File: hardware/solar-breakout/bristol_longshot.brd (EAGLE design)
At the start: 67 parts, among them U1 SPV1040, U2 SPV1040, U3 LT4054ES5-4.2, U4 TPS62243, U5 TPS62243, U6 TPS3808, U7 74LVC1G04GW

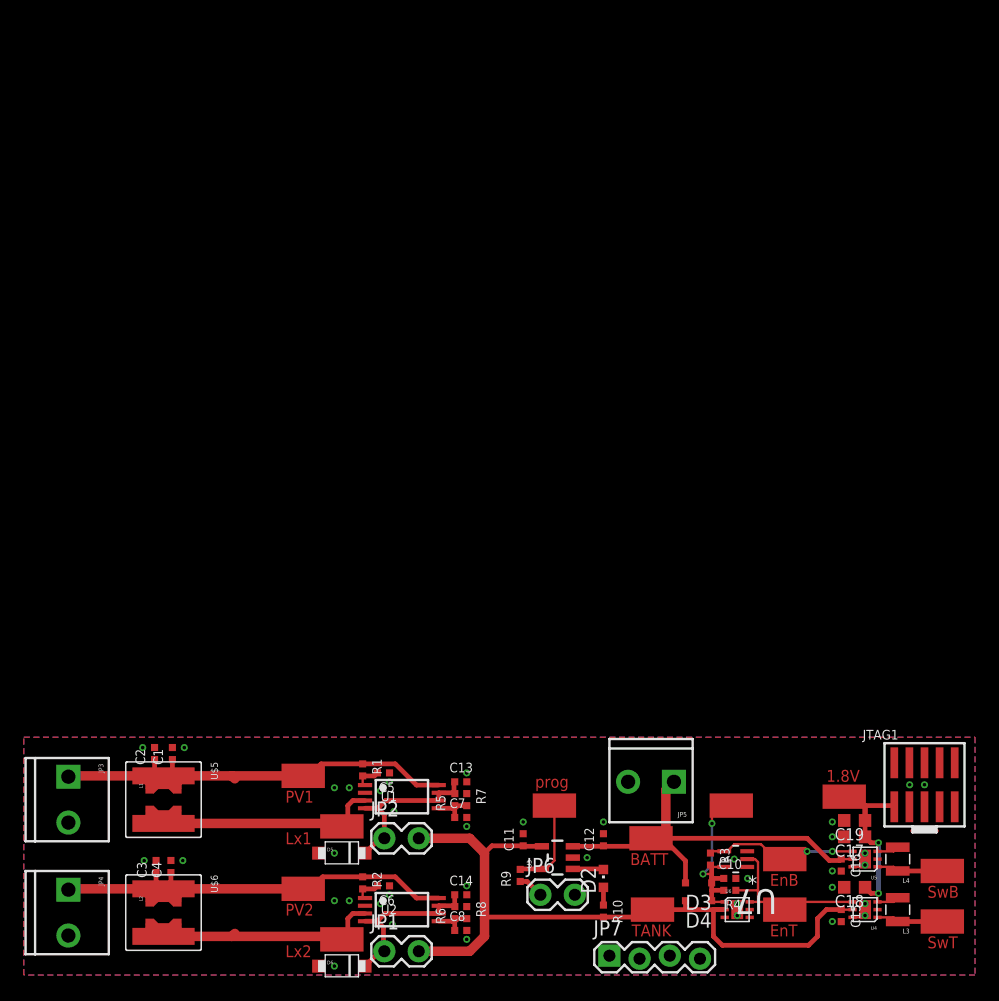
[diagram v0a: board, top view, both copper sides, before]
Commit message: Update solar breakout to yet another design
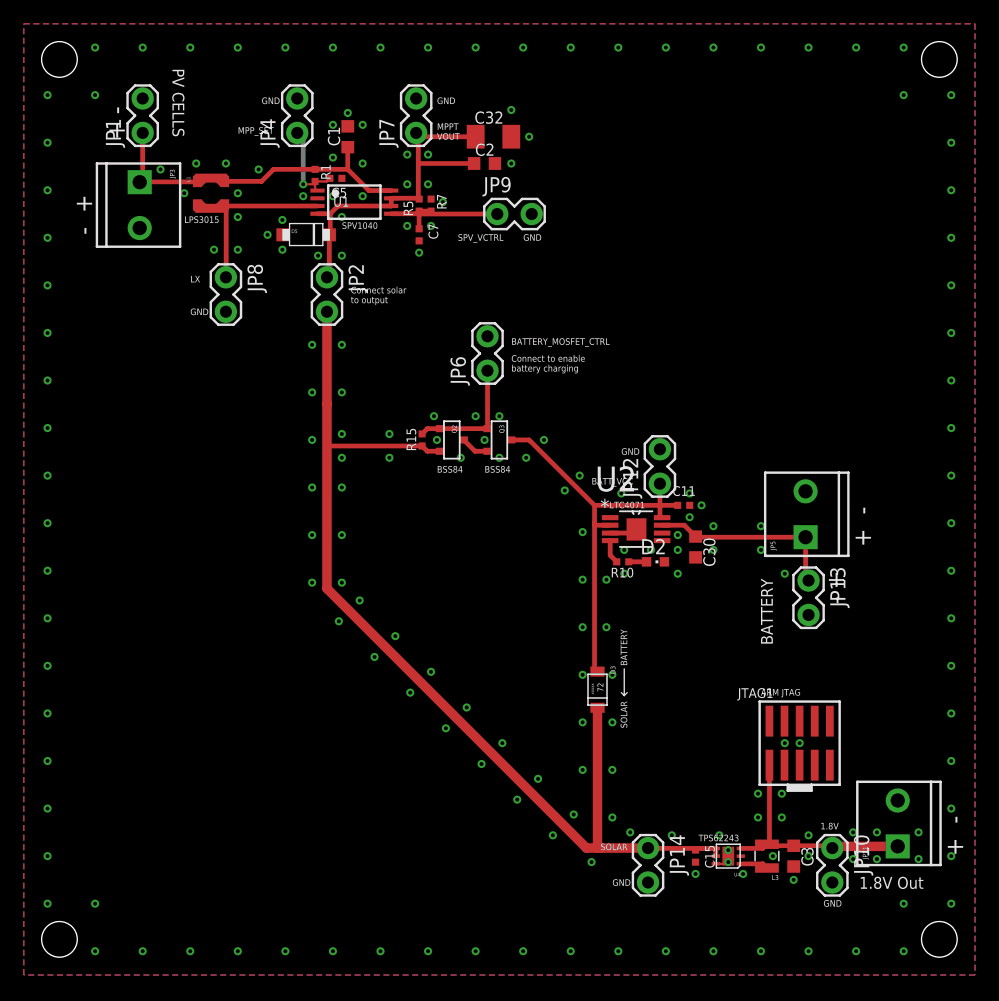
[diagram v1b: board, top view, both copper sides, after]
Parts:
- removed C10, C6, C8: 1nF, microbuilder_v3:_0402
- removed C12, C13, C14, C16, C4: 4.7µF, microbuilder_v3:_0402
- removed C17, C18, C19: 10µF, resistor:C0603K
- removed D4: BAT760, BAT760:SOD323
- removed D6: DIODE[TVS], nxp:SOD123W
- removed L2: 10uH LPS3015, PecanFemto4:LPS3015
- removed L4: 2.2µH, SparkFun:1007
- removed R2: 1kΩ, microbuilder_v3:_0402
- removed R3, R4: 10kΩ, microbuilder_v3:_0402
- removed R6: 220kΩ, microbuilder_v3:_0402
- removed R8: 82kΩ, microbuilder_v3:_0402
- removed R9: 2.2kΩ, microbuilder_v3:_0402
- removed U$25, U$30, U$31, U$33, U$34, U$39, U$41, U$42, U$43, U$44, U$45, U$46, U$47: S1751-46R, Harwin-Test-Point:S1751-46R
- removed U$5, U$6: XAL6060, XAL6060:XAL60
- removed U3: LT4054ES5-4.2, XYKlib:SOT23-5
- removed U5: TPS62243, TPS62243:S-PWSON-N6
- removed U6: TPS3808, TPS3808:S-PWSON-N6
- removed U7: 74LVC1G04GW, 74LVC1G04GW_inverter:SOT65P210X110-5N
- added C30: 10µF, resistor:C0603K
- added C32: 100µF, resistor:C1206K
- added JP10, JP12, JP13, JP14, JP8, JP9: (no value), SparkFun:1X02_LOCK
- added JP11: (no value), SparkFun:SCREWTERMINAL-3.5MM-2_LOCK
- added Q2, Q3: BSS84, nxp:SOT23
- added R15: 1MΩ, microbuilder_v3:_0402
- C1, C2, C3: value 4.7µF -> 10µF; device microbuilder_v3:_0402 -> resistor:C0603K
- C11, C15, C5, C7: device microbuilder_v3:_0402 -> microbuilder_v3:_0402@1
- D3: value BAT760 -> RB161M; device BAT760:SOD323 -> RB161M:RB161M
- JP4: value PV2 -> (none); device SparkFun:SCREWTERMINAL-3.5MM-2_LOCK -> SparkFun:1X02_LOCK
- JP6: value Shutdown -> (none)
- JP7: device SparkFun:1X04_LOCK -> SparkFun:1X02_LOCK
- U2: value SPV1040 -> LTC4071EMS8EPBF; device spv1040:TSSOP8 -> LTC4071_EMS8:SOP65P490X110-9N
- moved JP1 72.0 mm to (10.0, 71.0), turned to 90 degrees
- moved JP7 71.4 mm to (33.0, 71.0), turned to 90 degrees
- moved JP4 66.8 mm to (23.0, 71.0), turned to 90 degrees
- moved C2 56.9 mm to (38.8, 68.2), turned to 0 degrees
- moved C1 53.9 mm to (27.2, 70.5)
- moved C3 53.6 mm to (64.8, 10.0), turned to 270 degrees
- moved D5 52.1 mm to (23.8, 62.2)
- moved L1 51.2 mm to (15.8, 65.8)
- moved JP3 50.4 mm to (9.75, 66.5)
- moved C5 50.2 mm to (26.2, 67.0)
- moved R1 50.2 mm to (24.5, 67.2)
- moved U1 50.2 mm to (25.5, 65.5)
- moved R5 50.1 mm to (33.2, 64.8)
- moved R7 50.1 mm to (34.2, 64.8)
- moved C7 49.1 mm to (33.2, 62.2), turned to 270 degrees
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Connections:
- removed net BATTERY_BUCK_SW: L4.1, U$46.PAD, U5.1
- removed net BATTERY_EN: R3.1, U$44.PAD, U5.4, U7.4
- removed net CHG: D2.C, U3.1
- removed net CT: U6.3
- removed net LX1: L1.2_1, L1.2_2, L1.2_3, L1.2_4, L1.2_5, L1.2_6, L1.2_7, L1.2_8, L1.2_9, U$33.PAD, U$5.P$2, U1.3
- removed net LX2: L2.2_1, L2.2_2, L2.2_3, L2.2_4, L2.2_5, L2.2_6, L2.2_7, L2.2_8, L2.2_9, U$34.PAD, U$6.P$2, U2.3
- removed net MPP-SET2: C6.2, R2.2, U2.1
- removed net MPPT-VOUT-1: C13.1, D5.P$2, JP2.1, R5.2, U1.4, U1.6, U1.7
- removed net MPPT-VOUT-2: C14.1, D6.P$2, JP1.1, R6.2, U2.4, U2.6, U2.7
- removed net N$1: C5.2, R1.2, U1.1
- removed net N$5: JP6.1, R9.1
- removed net PROG: R9.2, U$25.PAD, U3.5
- removed net PV1: C1.1, C2.1, JP3.1, L1.1_1, L1.1_2, L1.1_3, L1.1_4, L1.1_5, L1.1_6, L1.1_7, L1.1_8, L1.1_9, R1.1, U$30.PAD, U$5.P$1, U1.8
- removed net PV2: C3.1, C4.1, JP4.1, L2.1_1, L2.1_2, L2.1_3, L2.1_4, L2.1_5, L2.1_6, L2.1_7, L2.1_8, L2.1_9, R2.1, U$31.PAD, U$6.P$1, U2.8
- removed net SPV_VCTRL1: C7.1, R5.1, R7.2, U1.5
- removed net SPV_VCTRL2: C8.1, R6.1, R8.2, U2.5
- removed net SUPERVISOR_VCC: C10.1, D3.C, D4.C, R3.2, R4.2, U$47.PAD, U6.1, U7.5
- removed net TANK: C11.1, C15.1, D4.A, JP1.2, JP2.2, R10.2, U$41.PAD, U3.4, U4.5, U6.2
- removed net TANK_BUCK_SW: L3.1, U$45.PAD, U4.1
- removed net TANK_EN: R4.1, U$43.PAD, U4.4, U6.6, U7.2
- new net BATTERY_MOSFET_1: Q2.3, Q3.2
- new net BATTERY_VCC: C11.1, D3.ANODE, JP12.1, Q3.3, U2.2, U2.8
- new net BATT_MOSFET_CTRL: JP6.1, Q2.1, Q3.1, R15.2
- new net HBO: R10.2, U2.4
- new net LX: JP8.1, L1.2_1, L1.2_2, L1.2_3, L1.2_4, L1.2_5, L1.2_6, L1.2_7, L1.2_8, L1.2_9, U1.3
- new net MPPT_VOUT: C2.1, C32.1, D5.P$2, JP2.1, JP7.1, R5.2, U1.4, U1.6, U1.7
- new net MPP_SET: C5.2, JP4.1, R1.2, U1.1
- new net N$7: L3.1, U4.1
- new net PV: C1.1, JP1.1, JP3.1, L1.1_1, L1.1_2, L1.1_3, L1.1_4, L1.1_5, L1.1_6, L1.1_7, L1.1_8, L1.1_9, R1.1, U1.8
- new net SOLAR: C15.1, D3.CATHODE, JP14.1, JP2.2, Q2.2, R15.1, U4.4, U4.5
- new net SPV_VCTRL: C7.1, JP9.1, R5.1, R7.2, U1.5
- net 1.8V: now also C3.1, JP10.1, JP11.1; no longer C17.1, C18.1, C19.1, L4.2, U$42.PAD, U5.3
- net BATTERY: now also C30.1, JP13.1, U2.7; no longer C12.1, C16.1, D3.A, U$39.PAD, U3.3, U5.5
- net GND: now also C30.2, C32.2, D2.C, JP1.2, JP10.2, JP11.2, JP12.2, JP13.2, JP14.2, JP8.2, JP9.2, U2.3, U2.5, U2.6, U2.9; no longer C10.2, C12.2, C13.2, C14.2, C16.2, C17.2, C18.2, C19.2, C4.2, C6.1, C8.2, D6.P$1, JP7.1, JP7.3, JP7.4, R8.1, U2.2, U3.2, U5.2, U5.6, U5.PAD, U6.5, U6.PAD, U7.3
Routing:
- net SOLAR: track 0.00 -> 92.5 mm
- net TANK: track 63.3 -> 0.00 mm
- net PV1: track 41.8 -> 0.00 mm
- net PV2: track 40.7 -> 0.00 mm
- net BATTERY_VCC: track 0.00 -> 34.9 mm
- net PV: track 0.00 -> 31.0 mm
- net MPPT_VOUT: track 0.00 -> 30.0 mm
- net LX2: track 24.2 -> 0.00 mm
- net LX1: track 24.1 -> 0.00 mm
- net LX: track 0.00 -> 18.5 mm
- net BATTERY: track 34.6 -> 16.2 mm
- net SUPERVISOR_VCC: track 16.1 -> 0.00 mm, vias 2 -> 0
- net TANK_EN: track 15.4 -> 0.00 mm
- net MPPT-VOUT-2: track 14.4 -> 0.00 mm
- net MPPT-VOUT-1: track 14.3 -> 0.00 mm
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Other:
- board text added: "+ -"
- board text added: "- +"
- board text added: "1.8V Out"
- board text added: "ARM JTAG"
- board text added: "BATTERY"
- board text added: "BATTERY_MOSFET_CTRL"
- board text added: "BATT_VCC"
- board text added: "BSS84"
- board text added: "Connect solar to output"
- board text added: "Connect to enable battery charging"
- board text added: "GND"
- board text added: "LPS3015"
- board text added: "LTC4071"
- board text added: "LX"
- board text added: "MPPT VOUT"
- board text added: "MPP_SET"
- board text added: "PV CELLS"
- board text added: "SOLAR"
- board text added: "SPV1040"
- board text added: "SPV_VCTRL"
- board text added: "TPS62243"
- board text removed: "BATT"
- board text removed: "EnB"
- board text removed: "EnT"
- board text removed: "Lx1"
- board text removed: "Lx2"
- board text removed: "PV1"
- board text removed: "PV2"
- board text removed: "SwB"
- board text removed: "SwT"
- board text removed: "TANK"
- board text removed: "prog"

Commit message: Added dimension
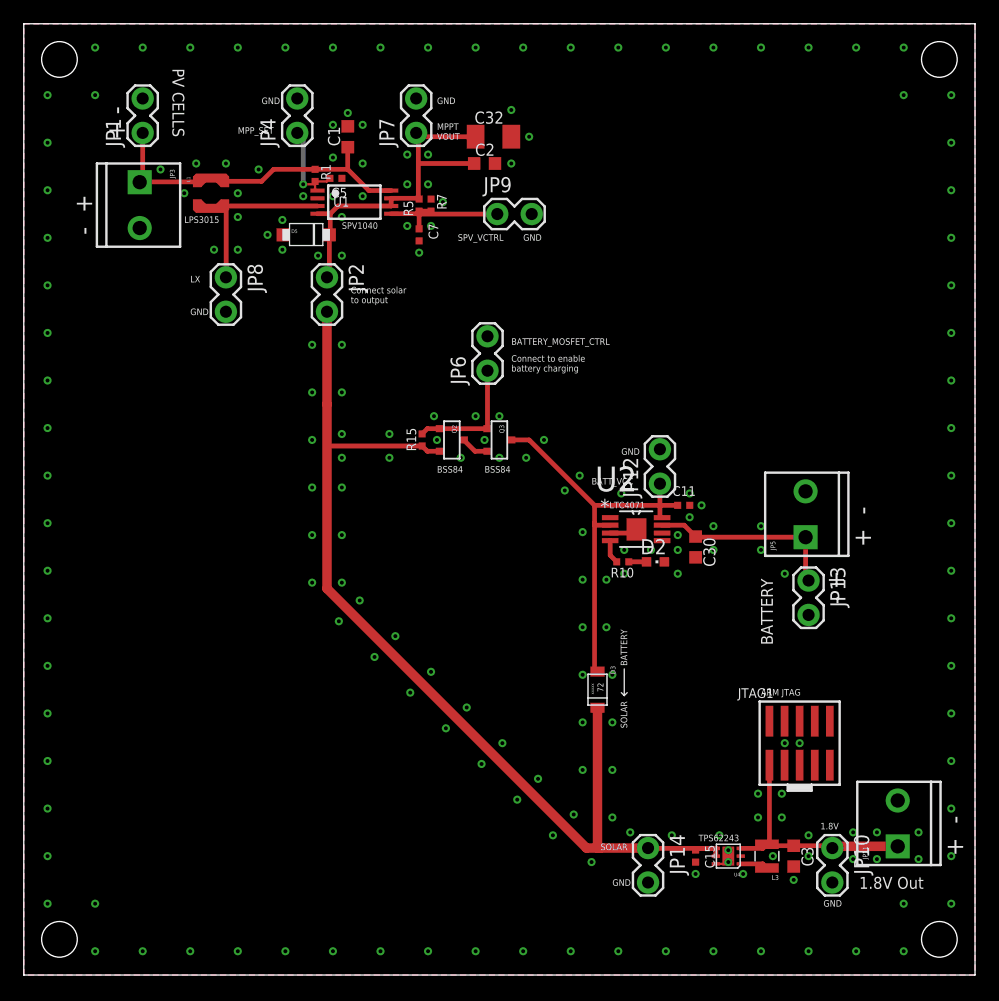
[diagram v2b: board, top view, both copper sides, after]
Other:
- board outline added: 80 x 80 mm
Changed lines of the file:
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@@
 <setting verticaltext="up"/>
 </settings>
-<grid distance="0.25" unitdist="mm" unit="mm" style="lines" multiple="1" display="yes" altdistance="0.025" altunitdist="inch" altunit="inch"/>
+<grid distance="10" unitdist="mm" unit="mm" style="lines" multiple="1" display="yes" altdistance="0.025" altunitdist="inch" altunit="inch"/>
 <layers>
 <layer number="1" name="Top" color="4" fill="1" visible="yes" active="yes"/>
@@
 battery charging</text>
 <text x="56.75" y="11.25" size="0.55" layer="21" font="vector" ratio="14">TPS62243</text>
+<wire x1="0" y1="80" x2="80" y2="80" width="0" layer="20"/>
+<wire x1="80" y1="80" x2="80" y2="0" width="0" layer="20"/>
+<wire x1="80" y1="0" x2="0" y2="0" width="0" layer="20"/>
+<wire x1="0" y1="0" x2="0" y2="80" width="0" layer="20"/>
 </plain>
 <attributes>

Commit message: [solar-breakout] replace LTC4071 -> LTC4070 as tested
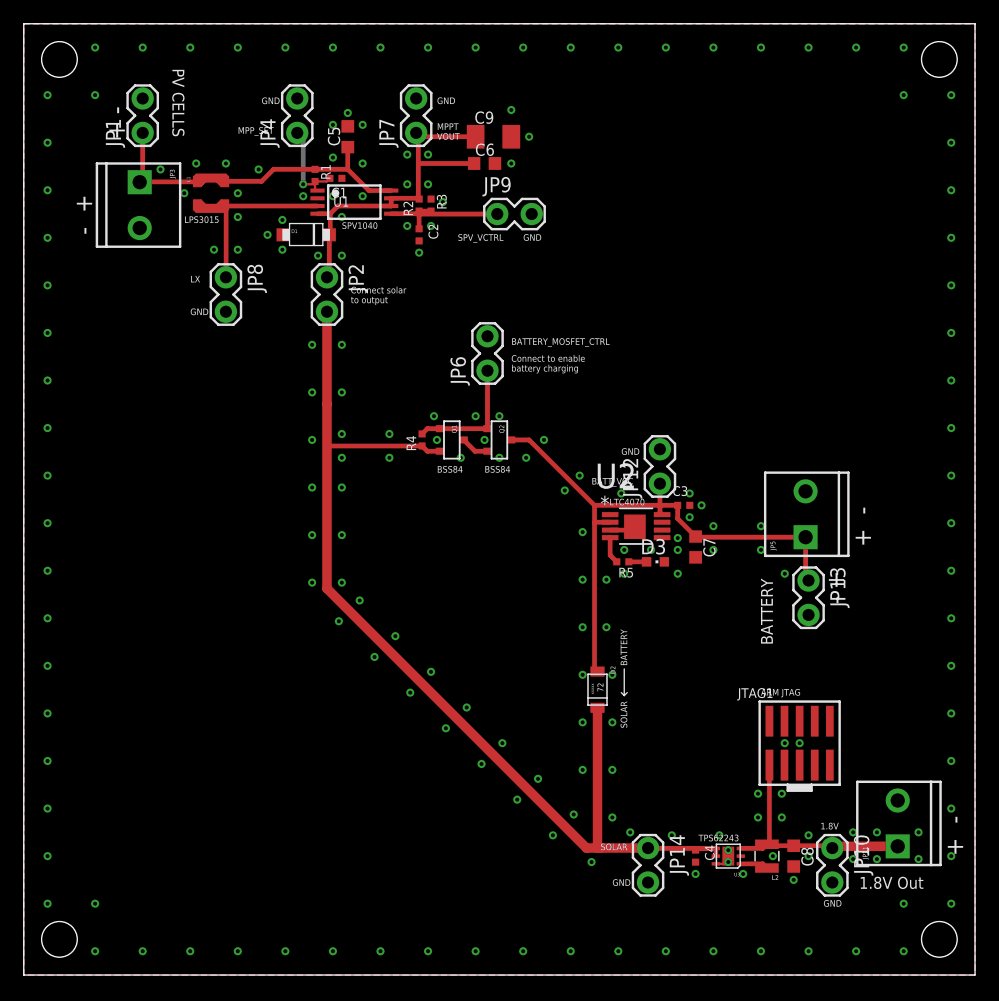
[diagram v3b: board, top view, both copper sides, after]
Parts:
- removed C11: 4.7µF, microbuilder_v3:_0402@1
- removed C30: 10µF, resistor:C0603K
- removed Q3: BSS84, nxp:SOT23
- removed R10: 330Ω, microbuilder_v3:_0402
- added C6, C8: 10µF, resistor:C0603K
- added Q1: BSS84, nxp:SOT23
- added R2: 220kΩ, microbuilder_v3:_0402
- C1, C2: value 10µF -> 1nF; device resistor:C0603K -> microbuilder_v3:_0402@1
- C3: value 10µF -> 1µF; device resistor:C0603K -> microbuilder_v3:_0402@1
- C5, C7: value 1nF -> 10µF; device microbuilder_v3:_0402@1 -> resistor:C0603K
- D2: value GREEN -> RB161M; device led:CHIPLED_0603 -> RB161M:RB161M
- D3: value RB161M -> GREEN; device RB161M:RB161M -> led:CHIPLED_0603
- R5: value 220kΩ -> 330Ω
- U2: value LTC4071EMS8EPBF -> LTC4070EMS8EPBF; device LTC4071_EMS8:SOP65P490X110-9N -> LTC4070_EMS8:SOP65P490X110-9N
- moved C7 35.1 mm to (56.5, 36.0)
- moved R5 34.5 mm to (50.4, 34.8), turned to 180 degrees
- moved C3 30.9 mm to (55.5, 39.5), turned to 0 degrees
- moved D2 11.8 mm to (48.2, 24.0), turned to 180 degrees
- moved D3 11.8 mm to (53.1, 34.8), turned to 270 degrees
- moved C2 8.14 mm to (33.2, 62.2), turned to 270 degrees
- moved Q2 4.00 mm to (40.0, 45.0)
- moved C1 3.64 mm to (26.2, 67.0), turned to 180 degrees
- moved C5 3.64 mm to (27.2, 70.5), turned to 90 degrees
- moved U2 0.25 mm to (51.5, 37.8)
- renumbered C15 to C4, C32 to C9, D5 to D1, L3 to L2, R15 to R4, R7 to R3, U4 to U3
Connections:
- removed net BATTERY_VCC: C11.1, D3.ANODE, JP12.1, Q3.3, U2.2, U2.8
- new net NTCBIAS: U2.1
- net 1.8V: now also C8.1; no longer C3.1
- net BATTERY: now also C3.1, C7.1, D2.ANODE, JP12.1, Q2.3, U2.2, U2.8; no longer C30.1, U2.7
- net BATTERY_MOSFET_1: now also Q1.3, Q2.2; no longer Q2.3, Q3.2
- net BATT_MOSFET_CTRL: now also Q1.1; no longer Q3.1
- net CHG_LED: now also D3.A, R5.1; no longer D2.A, R10.1
- net GND: now also C1.1, C5.2, C6.2, C8.2, D3.C; no longer C1.2, C11.2, C30.2, C5.1, D2.C, U2.6
- net HBO: now also R5.2; no longer R10.2
- net MPPT_VOUT: now also C6.1, R2.2; no longer C2.1, R5.2
- net MPP_SET: now also C1.2; no longer C5.2
- net PV: now also C5.1; no longer C1.1
- net SOLAR: now also D2.CATHODE, Q1.2; no longer D3.CATHODE, Q2.2
- net SPV_VCTRL: now also C2.1, R2.1; no longer C7.1, R5.1
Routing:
- net BATTERY_VCC: track 34.9 -> 0.00 mm
- net BATTERY: track 16.2 -> 50.8 mm
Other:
- board text added: "LTC4070"
- board text removed: "LTC4071"
